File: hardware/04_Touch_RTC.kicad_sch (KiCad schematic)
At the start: 27 parts, among them J7 FH12-6S-0.5SH(55) TOUCH, U11 TPS7A0230PDBVR, U12 SN74LVC1G07QDBVRQ1, U13 SN74LVC1G74-Q1 WAKE LATCH OPT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, U14 RV-3028-C7

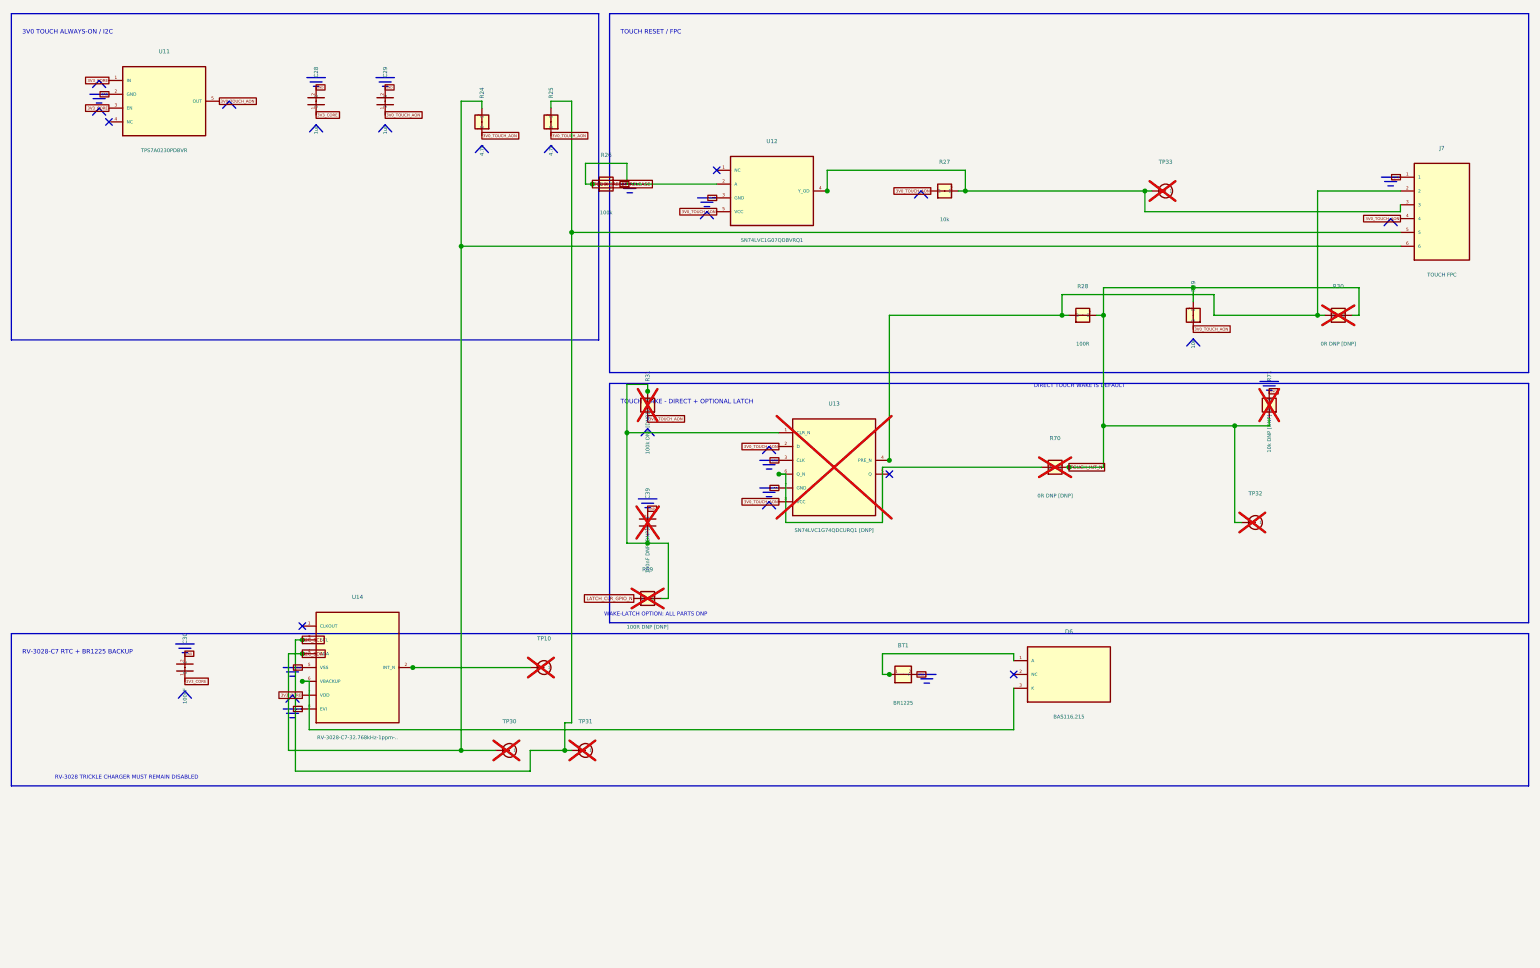
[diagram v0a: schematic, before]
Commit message: Rebuild Rev A schematic from a single verified circuit definition
- Requirements list extracted from spec v1.6 (docs/Anforderungsliste_RevA.md)
- New canonical circuit in scripts/rebuild/design.py with LCSC numbers
  (all stock-checked 2026-10-12) and generated 6-sheet KiCad schematic
- Power path kept on TI's automotive reference (LM74720-Q1 Fig. 9-1) with
  hold-up capacitor; buck moved to LMR33630C (2.1 MHz) for availability
- Fixes found during datasheet re-check: TPD2EUSB30 pinout, TPS25947 EN
  overvoltage and phantom EPAD, mirrored RV-3028 footprint, Good Display
  VSL capacitor, AL8861 VSET default, missing AUTOTERM_5V ESD, LED wire
  short-circuit protection
- ERC 0 violations; exported netlist matches the definition on all 668 pins

Co-Authored-By: Claude Opus 5.5 <noreply@anthropic.com>
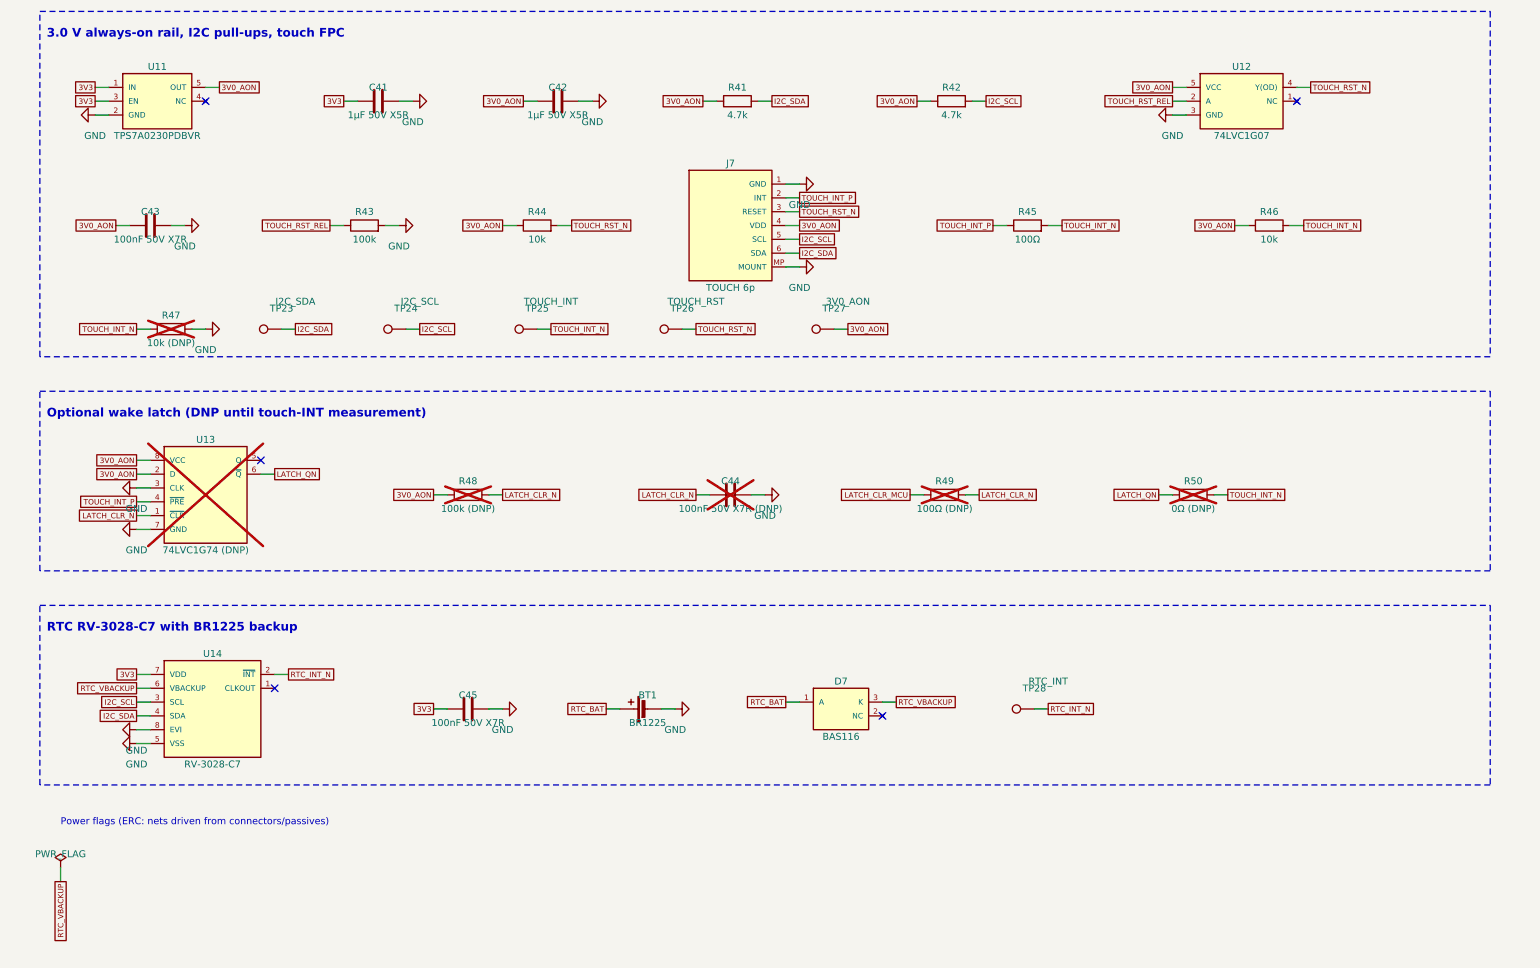
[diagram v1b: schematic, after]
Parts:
- removed BT1: BR1225 HOLDER, Battery:BatteryHolder_Keystone_500, symbol LandyHeater:BR1225_HOLDER_1__2
- removed C28, C29: 1uF, Capacitor_SMD:C_0603_1608Metric_Pad1.08x0.95mm_HandSolder, symbol LandyHeater:1uF_11_22
- removed C30: 100nF, Capacitor_SMD:C_0603_1608Metric_Pad1.08x0.95mm_HandSolder, symbol LandyHeater:100nF_11_22
- removed C39: 100nF DNP, Capacitor_SMD:C_0603_1608Metric_Pad1.08x0.95mm_HandSolder, symbol LandyHeater:100nF_DNP_11_22
- removed D6: BAS116,215, Package_TO_SOT_SMD:SOT-23, symbol LandyHeater:BAS116_215_1A_2NC_3K
- removed J7: FH12-6S-0.5SH(55) TOUCH, Connector_FFC-FPC:Hirose_FH12-6S-0.5SH_1x06-1MP_P0.50mm_Horizontal, symbol LandyHeater:FH12_6S_0_5SH_55_TOUCH_11_22_33_44_55_66
- removed R24, R25: 4.7k, Resistor_SMD:R_0603_1608Metric_Pad0.98x0.95mm_HandSolder, symbol LandyHeater:4_7k_11_22
- removed R26: 100k, Resistor_SMD:R_0603_1608Metric_Pad0.98x0.95mm_HandSolder, symbol LandyHeater:100k_11_22
- removed R27, R29: 10k, Resistor_SMD:R_0603_1608Metric_Pad0.98x0.95mm_HandSolder, symbol LandyHeater:10k_11_22
- removed R28: 100R, Resistor_SMD:R_0603_1608Metric_Pad0.98x0.95mm_HandSolder, symbol LandyHeater:100R_11_22
- removed R30, R70: 0R DNP, Resistor_SMD:R_0603_1608Metric_Pad0.98x0.95mm_HandSolder, symbol LandyHeater:0R_DNP_11_22
- removed R31: 100k DNP, Resistor_SMD:R_0603_1608Metric_Pad0.98x0.95mm_HandSolder, symbol LandyHeater:100k_DNP_11_22
- removed R69: 100R DNP, Resistor_SMD:R_0603_1608Metric_Pad0.98x0.95mm_HandSolder, symbol LandyHeater:100R_DNP_11_22
- removed R71: 10k DNP, Resistor_SMD:R_0603_1608Metric_Pad0.98x0.95mm_HandSolder, symbol LandyHeater:10k_DNP_11_22
- removed TP10: RTC_INT, TestPoint:TestPoint_Pad_D1.0mm, symbol LandyHeater:RTC_INT_11
- removed TP30: I2C_SDA, TestPoint:TestPoint_Pad_D1.0mm, symbol LandyHeater:I2C_SDA_11
- removed TP31: I2C_SCL, TestPoint:TestPoint_Pad_D1.0mm, symbol LandyHeater:I2C_SCL_11
- removed TP32: TOUCH_INT_N, TestPoint:TestPoint_Pad_D1.0mm, symbol LandyHeater:TOUCH_INT_N_11
- removed TP33: TOUCH_RESET_N, TestPoint:TestPoint_Pad_D1.0mm, symbol LandyHeater:TOUCH_RESET_N_11
- removed U11: TPS7A0230PDBVR, Package_TO_SOT_SMD:SOT-23-5, symbol LandyHeater:TPS7A0230PDBVR_1IN_2GND_3EN_4NC_5OUT
- removed U12: SN74LVC1G07QDBVRQ1, Package_TO_SOT_SMD:SOT-23-5, symbol LandyHeater:SN74LVC1G07QDBVRQ1_1NC_2A_3GND_4Y_OD_5VCC
- removed U13: SN74LVC1G74-Q1 WAKE LATCH OPTION, Package_SO:VSSOP-8_2.3x2mm_P0.5mm, symbol LandyHeater:SN74LVC1G74_Q1_WAKE_LATCH_OPTION_1CLR_N_2D_3CLK_4PRE_N_5Q_6Q_N_7GND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
- removed U14: RV-3028-C7, LandyHeater:RV-3028-C7, symbol LandyHeater:RV_3028_C7_1CLKOUT_2INT_N_3SCL_4SDA_5VSS_6VBACKUP_7VDD_8EVI
- added BT1: BR1225, Battery:BatteryHolder_LINX_BAT-HLD-012-SMT, symbol Device:Battery_Cell
- added C41, C42: 1µF 50V X5R, Capacitor_SMD:C_0603_1608Metric, symbol Device:C
- added C43, C45: 100nF 50V X7R, Capacitor_SMD:C_0603_1608Metric, symbol Device:C
- added C44: 100nF 50V X7R (DNP), Capacitor_SMD:C_0603_1608Metric, symbol Device:C
- added D7: BAS116, Package_TO_SOT_SMD:SOT-23, symbol LandyHeater_RevA:D_SOT23
- added J7: TOUCH 6p, Connector_FFC-FPC:Hirose_FH12-6S-0.5SH_1x06-1MP_P0.50mm_Horizontal, symbol LandyHeater_RevA:CONN_FPC6
- added R41, R42: 4.7k, Resistor_SMD:R_0603_1608Metric, symbol Device:R
- added R43: 100k, Resistor_SMD:R_0603_1608Metric, symbol Device:R
- added R44, R46: 10k, Resistor_SMD:R_0603_1608Metric, symbol Device:R
- added R45: 100Ω, Resistor_SMD:R_0603_1608Metric, symbol Device:R
- added R47: 10k (DNP), Resistor_SMD:R_0603_1608Metric, symbol Device:R
- added R48: 100k (DNP), Resistor_SMD:R_0603_1608Metric, symbol Device:R
- added R49: 100Ω (DNP), Resistor_SMD:R_0603_1608Metric, symbol Device:R
- added R50: 0Ω (DNP), Resistor_SMD:R_0603_1608Metric, symbol Device:R
- added TP23: I2C_SDA, TestPoint:TestPoint_Pad_D1.0mm, symbol Connector:TestPoint
- added TP24: I2C_SCL, TestPoint:TestPoint_Pad_D1.0mm, symbol Connector:TestPoint
- added TP25: TOUCH_INT, TestPoint:TestPoint_Pad_D1.0mm, symbol Connector:TestPoint
- added TP26: TOUCH_RST, TestPoint:TestPoint_Pad_D1.0mm, symbol Connector:TestPoint
- added TP27: 3V0_AON, TestPoint:TestPoint_Pad_D1.0mm, symbol Connector:TestPoint
- added TP28: RTC_INT, TestPoint:TestPoint_Pad_D1.0mm, symbol Connector:TestPoint
- added U11: TPS7A0230PDBVR, Package_TO_SOT_SMD:SOT-23-5, symbol LandyHeater_RevA:TPS7A02
- added U12: 74LVC1G07, Package_TO_SOT_SMD:SOT-23-5, symbol LandyHeater_RevA:LVC1G07
- added U13: 74LVC1G74 (DNP), Package_SO:VSSOP-8_2.3x2mm_P0.5mm, symbol LandyHeater_RevA:LVC1G74
- added U14: RV-3028-C7, LandyHeater_RevA:MicroCrystal_RV-3028-C7, symbol LandyHeater_RevA:RV3028
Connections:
- net GND: now also BT1.2 (-), C41.2, C42.2, C43.2, C44.2, C45.2, J7.1 (GND), J7.MP (MOUNT), R43.2, R47.2, U11.2 (GND), U12.3 (GND), U13.3 (CLK), U13.7 (GND), U14.5 (VSS), U14.8 (EVI)
- net I2C_SCL: now also J7.5 (SCL), R42.2, TP24.1, U14.3 (SCL)
- net I2C_SDA: now also J7.6 (SDA), R41.2, TP23.1, U14.4 (SDA)
- net TOUCH_INT_N: now also R45.2, R46.2, R47.1, R50.2, TP25.1
- new net 3V0_AON: C42.1, C43.1, J7.4 (VDD), R41.1, R42.1, R44.1, R46.1, R48.1, TP27.1, U11.5 (OUT), U12.5 (VCC), U13.2 (D), U13.8 (VCC)
- new net 3V3: C41.1, C45.1, U11.1 (IN), U11.3 (EN), U14.7 (VDD)
- new net LATCH_CLR_MCU: R49.1
- new net LATCH_CLR_N: C44.1, R48.2, R49.2, U13.1 (~{CLR})
- new net LATCH_QN: R50.1, U13.6 (~{Q})
- new net RTC_BAT: BT1.1 (+), D7.1 (A)
- new net RTC_INT_N: TP28.1, U14.2 (~{INT})
- new net RTC_VBACKUP: D7.3 (K), U14.6 (VBACKUP)
- new net TOUCH_INT_P: J7.2 (INT), R45.1, U13.4 (~{PRE})
- new net TOUCH_RST_N: J7.3 (RESET), R44.2, TP26.1, U12.4 (Y(OD))
- new net TOUCH_RST_REL: R43.1, U12.2 (A)
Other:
- note added: "3.0 V always-on rail, I2C pull-ups, touch FPC"
- note added: "Optional wake latch (DNP until touch-INT measurement)"
- note added: "Power flags (ERC: nets driven from connectors/passives)"
- note added: "RTC RV-3028-C7 with BR1225 backup"
- note removed: "3V0 TOUCH ALWAYS-ON / I2C"
- note removed: "DIRECT TOUCH WAKE IS DEFAULT"
- note removed: "RV-3028 TRICKLE CHARGER MUST REMAIN DISABLED"
- note removed: "RV-3028-C7 RTC + BR1225 BACKUP"
- note removed: "TOUCH RESET / FPC"
- note removed: "TOUCH WAKE - DIRECT + OPTIONAL LATCH"
- note removed: "WAKE-LATCH OPTION: ALL PARTS DNP"
- title: Touch always-on rail and RTC -> LandyHeater-Board Rev A – Touch always-on rail and RTC

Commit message: Place Rev A board: 4-layer stackup, zones, two-sided placement
Generated by scripts/rebuild/gen_pcb.py from the same circuit definition.
Pre-route DRC: 0 errors, schematic parity: 0 issues.

Co-Authored-By: Claude Opus 5.5 <noreply@anthropic.com>
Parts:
- C44: value 100nF 50V X7R (DNP) -> 100nF 50V X7R
- R47: value 10k (DNP) -> 10k
- R48: value 100k (DNP) -> 100k
- R49: value 100Ω (DNP) -> 100Ω
- R50: value 0Ω (DNP) -> 0Ω
- U13: value 74LVC1G74 (DNP) -> 74LVC1G74
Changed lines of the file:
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@@
 			)
 		)
-		(property "Value" "10k (DNP)"
+		(property "Value" "10k"
 			(at 39.37 82.55 270)
 			(effects
@@
 			)
 		)
-		(property "Value" "74LVC1G74 (DNP)"
+		(property "Value" "74LVC1G74"
 			(at 45.72 120.65 0)
 			(effects
@@
 			)
 		)
-		(property "Value" "100k (DNP)"
+		(property "Value" "100k"
 			(at 93.98 113.03 270)
 			(effects
@@
 			)
 		)
-		(property "Value" "100nF 50V X7R (DNP)"
+		(property "Value" "100nF 50V X7R"
 			(at 142.24 113.03 270)
 			(effects
@@
 			)
 		)
-		(property "Value" "100Ω (DNP)"
+		(property "Value" "100Ω"
 			(at 181.61 113.03 270)
 			(effects
@@
 			)
 		)
-		(property "Value" "0Ω (DNP)"
+		(property "Value" "0Ω"
 			(at 227.33 113.03 270)
 			(effects
